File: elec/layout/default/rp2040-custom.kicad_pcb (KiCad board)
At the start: 2 copper layers, 40 x 40 mm, 28 parts

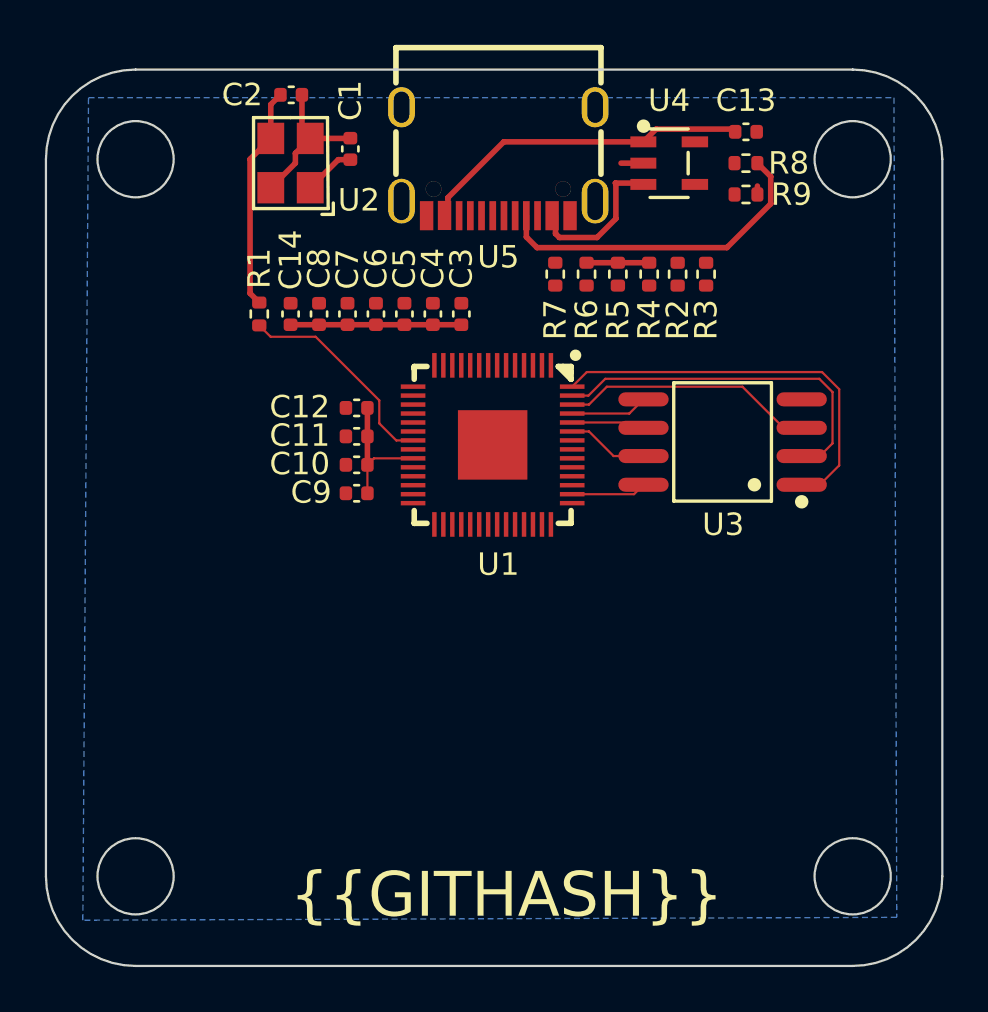
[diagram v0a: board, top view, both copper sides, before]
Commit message: remove misplaced kicad prj
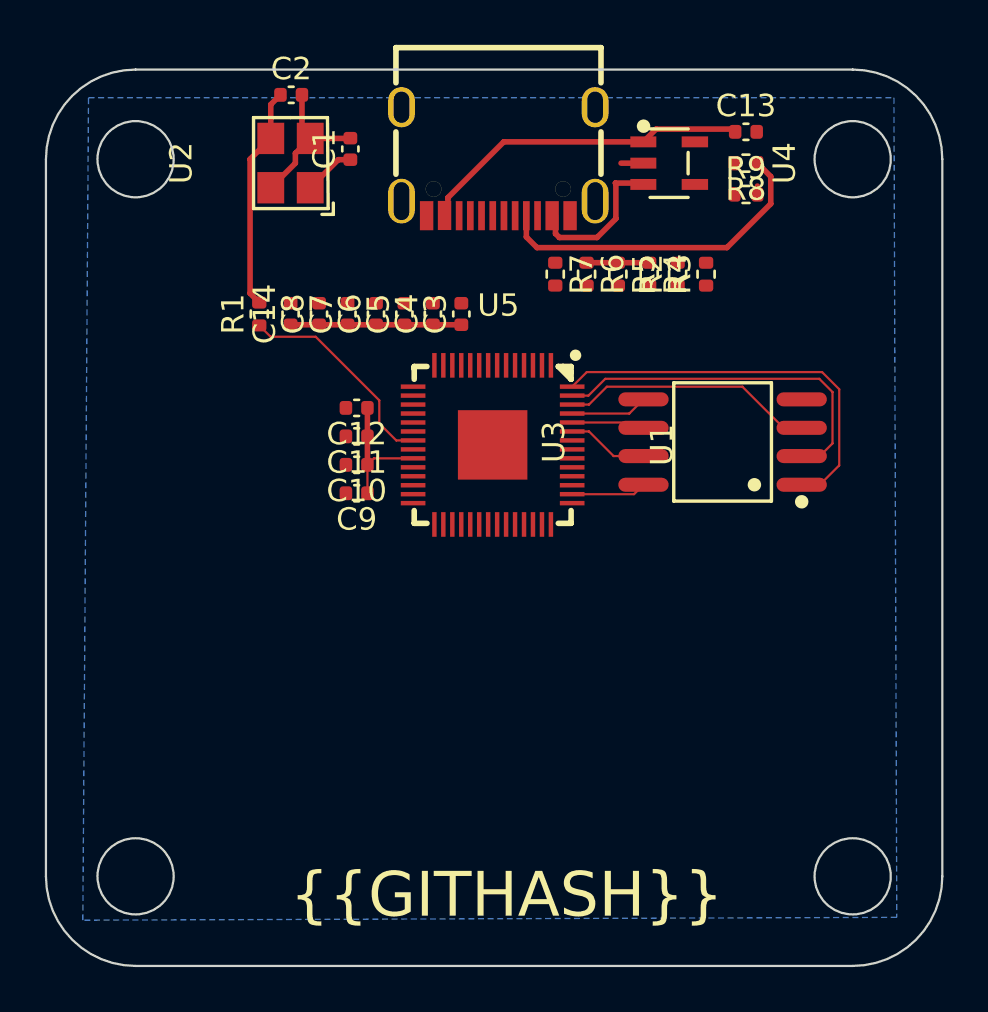
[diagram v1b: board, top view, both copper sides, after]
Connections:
- net CC1 renamed cc1
- net CC2 renamed cc2
- net SUB1 renamed sub1
- net SUB2 renamed sub2
- net cs-1 renamed gpio9
- net io renamed out-1
- net miso renamed gpio8
- net mosi renamed gpio11
- net sck-1 renamed gpio10
- net scl renamed gpio21
- net sda renamed gpio20
- net vcc-3 renamed out
- C1 pad 1: vcc-2 -> xin
- C13 pad 1: vcc-4 -> vcc-2
- C13 pad 2: gnd-4 -> gnd
- R8 pad 2: gnd-4 -> gnd
- R9 pad 2: gnd-4 -> gnd
- U1 pad 20: vcc-2 -> xin
- U2 pad 1: vcc-2 -> xin
- U4 pad 1: vcc-4 -> vcc-2
- U4 pad 2: gnd-4 -> gnd
- U4 pad 3: vcc-4 -> vcc-2
- U5 pad 1: gnd-4 -> gnd
- U5 pad 2: gnd-4 -> gnd
- U5 pad 3: gnd-4 -> gnd
- U5 pad 4: gnd-4 -> gnd
- U5 pad A1: gnd-4 -> gnd
- U5 pad A12: gnd-4 -> gnd
- U5 pad A4: vcc-4 -> vcc-2
- U5 pad A9: vcc-4 -> vcc-2
- U5 pad B1: gnd-4 -> gnd
- U5 pad B12: gnd-4 -> gnd
- U5 pad B4: vcc-4 -> vcc-2
- U5 pad B9: vcc-4 -> vcc-2
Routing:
- net vcc-4: track 21.8 -> 0.00 mm
- net vcc-2: track 2.31 -> 21.8 mm
- net xin: track 0.00 -> 2.31 mm
- net gnd-4: track 1.91 -> 0.00 mm
- net gnd: track 8.24 -> 10.1 mm
